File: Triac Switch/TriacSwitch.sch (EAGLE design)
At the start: 14 parts, among them T2 BT136

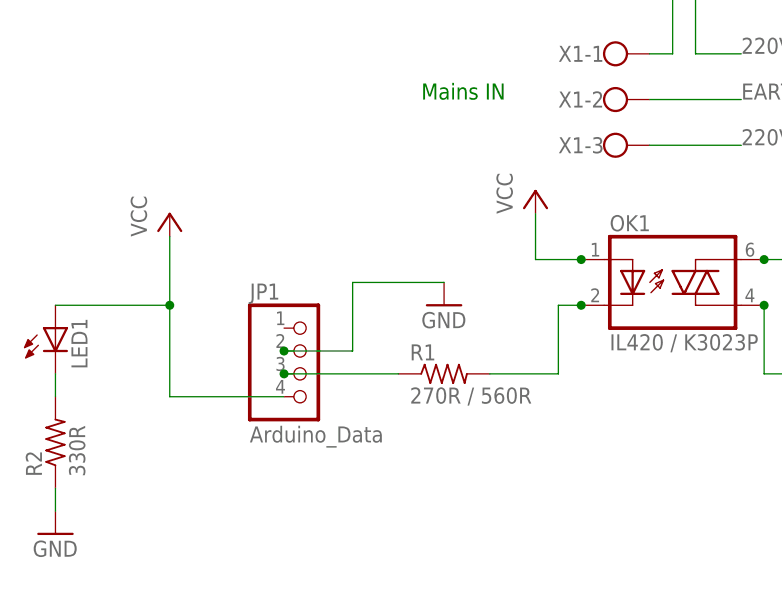
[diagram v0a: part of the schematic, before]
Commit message: Added Pinout to UD001 (Vishay) after successful test
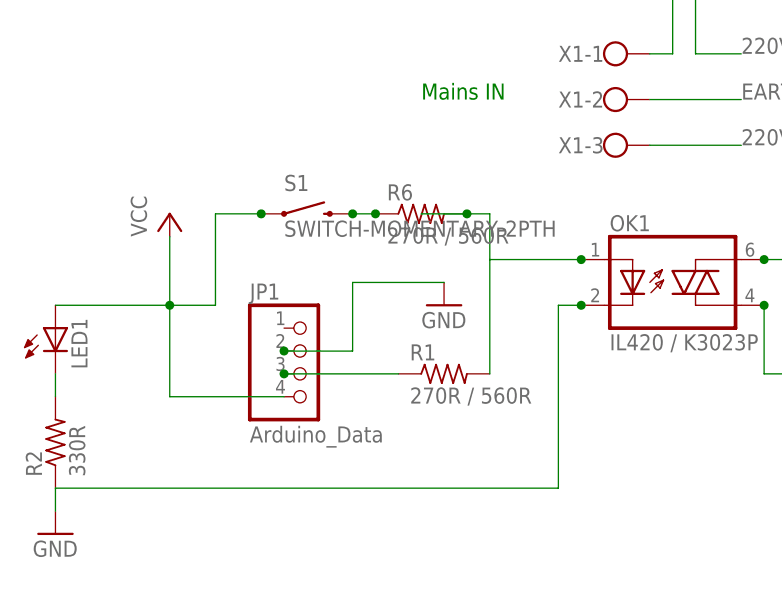
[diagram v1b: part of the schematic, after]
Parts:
- added R6: 270R / 560R, resistor:R-US_0207/10
- added S1: SWITCH-MOMENTARY-2PTH, SparkFun-Electromechanical:SWITCH-MOMENTARY-2PTH
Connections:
- removed net N$10: OK1.C, R1.2
- new net N$5: R6.1, S1.2
- new net N$8: OK1.A, R1.2, R6.2
- net GND: now also OK1.C
- net VCC: now also S1.1; no longer OK1.A
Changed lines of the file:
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@@
 <layers>
 <layer number="1" name="Top" color="4" fill="1" visible="no" active="no"/>
+<layer number="2" name="Route2" color="1" fill="3" visible="no" active="no"/>
+<layer number="3" name="Route3" color="4" fill="3" visible="no" active="no"/>
+<layer number="4" name="Route4" color="1" fill="4" visible="no" active="no"/>
+<layer number="5" name="Route5" color="4" fill="4" visible="no" active="no"/>
+<layer number="6" name="Route6" color="1" fill="8" visible="no" active="no"/>
+<layer number="7" name="Route7" color="4" fill="8" visible="no" active="no"/>
+<layer number="8" name="Route8" color="1" fill="2" visible="no" active="no"/>
+<layer number="9" name="Route9" color="4" fill="2" visible="no" active="no"/>
+<layer number="10" name="Route10" color="1" fill="7" visible="no" active="no"/>
+<layer number="11" name="Route11" color="4" fill="7" visible="no" active="no"/>
+<layer number="12" name="Route12" color="1" fill="5" visible="no" active="no"/>
+<layer number="13" name="Route13" color="4" fill="5" visible="no" active="no"/>
+<layer number="14" name="Route14" color="1" fill="6" visible="no" active="no"/>
+<layer number="15" name="Route15" color="4" fill="6" visible="no" active="no"/>
 <layer number="16" name="Bottom" color="1" fill="1" visible="no" active="no"/>
 <layer number="17" name="Pads" color="2" fill="1" visible="no" active="no"/>
@@
 <layer number="51" name="tDocu" color="7" fill="1" visible="no" active="no"/>
 <layer number="52" name="bDocu" color="7" fill="1" visible="no" active="no"/>
+<layer number="53" name="tGND_GNDA" color="7" fill="9" visible="no" active="no"/>
+<layer number="54" name="bGND_GNDA" color="1" fill="9" visible="no" active="no"/>
 <layer number="56" name="wert" color="7" fill="1" visible="no" active="no"/>
 <layer number="91" name="Nets" color="2" fill="1" visible="yes" active="yes"/>
@@
 <layer number="101" name="Gehäuse" color="7" fill="1" visible="no" active="yes"/>
 <layer number="102" name="Mittellin" color="7" fill="1" visible="no" active="yes"/>
+<layer number="103" name="tMap" color="7" fill="1" visible="no" active="yes"/>
 <layer number="104" name="Name" color="7" fill="1" visible="no" active="yes"/>
+<layer number="105" name="tPlate" color="7" fill="1" visible="no" active="yes"/>
+<layer number="106" name="bPlate" color="7" fill="1" visible="no" active="yes"/>
+<layer number="107" name="Crop" color="7" fill="1" visible="no" active="yes"/>
+<layer number="116" name="Patch_BOT" color="9" fill="4" visible="no" active="yes"/>
+<layer number="121" name="_tsilk" color="7" fill="1" visible="no" active="yes"/>
+<layer number="122" name="_bsilk" color="7" fill="1" visible="no" active="yes"/>
+<layer number="125" name="_tNames" color="7" fill="1" visible="no" active="yes"/>
+<layer number="144" name="Drill_legend" color="7" fill="1" visible="no" active="yes"/>
 <layer number="151" name="HeatSink" color="7" fill="1" visible="no" active="yes"/>
 <layer number="200" name="200bmp" color="1" fill="10" visible="no" active="no"/>
+<layer number="201" name="201bmp" color="2" fill="10" visible="no" active="yes"/>
+<layer number="202" name="202bmp" color="3" fill="10" visible="no" active="yes"/>
+<layer number="203" name="203bmp" color="4" fill="10" visible="no" active="yes"/>
+<layer number="204" name="204bmp" color="5" fill="10" visible="no" active="yes"/>
+<layer number="205" name="205bmp" color="6" fill="10" visible="no" active="yes"/>
+<layer number="206" name="206bmp" color="7" fill="10" visible="no" active="yes"/>
+<layer number="207" name="207bmp" color="8" fill="10" visible="no" active="yes"/>
+<layer number="208" name="208bmp" color="9" fill="10" visible="no" active="yes"/>
+<layer number="209" name="209bmp" color="7" fill="1" visible="no" active="yes"/>
+<layer number="210" name="210bmp" color="7" fill="1" visible="no" active="yes"/>
+<layer number="211" name="211bmp" color="7" fill="1" visible="no" active="yes"/>
+<layer number="212" name="212bmp" color="7" fill="1" visible="no" active="yes"/>
+<layer number="213" name="213bmp" color="7" fill="1" visible="no" active="yes"/>
+<layer number="214" name="214bmp" color="7" fill="1" visible="no" active="yes"/>
+<layer number="215" name="215bmp" color="7" fill="1" visible="no" active="yes"/>
+<layer number="216" name="216bmp" color="7" fill="1" visible="no" active="yes"/>
+<layer number="217" name="217bmp" color="18" fill="1" visible="no" active="no"/>
+<layer number="218" name="218bmp" color="19" fill="1" visible="no" active="no"/>
+<layer number="219" name="219bmp" color="20" fill="1" visible="no" active="no"/>
+<layer number="220" name="220bmp" color="21" fill="1" visible="no" active="no"/>
+<layer number="221" name="221bmp" color="22" fill="1" visible="no" active="no"/>
+<layer number="222" name="222bmp" color="23" fill="1" visible="no" active="no"/>
+<layer number="223" name="223bmp" color="24" fill="1" visible="no" active="no"/>
+<layer number="224" name="224bmp" color="25" fill="1" visible="no" active="no"/>
 <layer number="250" name="Descript" color="7" fill="1" visible="no" active="yes"/>
 <layer number="251" name="SMDround" color="7" fill="1" visible="no" active="yes"/>
@@
 <part name="JP1" library="pinhead" deviceset="PINHD-1X4" device="" value="Arduino_Data"/>
 <part name="P+1" library="supply1" deviceset="VCC" device=""/>
-<part name="P+2" library="supply1" deviceset="VCC" device=""/>
 <part name="GND1" library="supply1" deviceset="GND" device=""/>
 <part name="C1" library="cap-master" deviceset="CNP-" device="C050-110X055" value="100nF"/>
@@
 <part name="R5" library="resistor" deviceset="R-US_" device="0617/17" value="15K 5W"/>
 <part name="R3" library="resistor" deviceset="R-US_" device="0922/22" value="390R 10W"/>
+<part name="S1" library="SparkFun-Electromechanical" deviceset="SWITCH-MOMENTARY-2" device="PTH"/>
+<part name="R6" library="resistor" deviceset="R-US_" device="0207/10" value="270R / 560R"/>
 </parts>
 <sheets>
@@
 <instance part="JP1" gate="A" x="35.56" y="48.26"/>
 <instance part="P+1" gate="VCC" x="20.32" y="66.04"/>
-<instance part="P+2" gate="VCC" x="60.96" y="68.58"/>
 <instance part="GND1" gate="1" x="50.8" y="55.88"/>
 <instance part="C1" gate="G$1" x="139.7" y="50.8" rot="R90"/>
@@
 <instance part="R5" gate="G$1" x="99.06" y="60.96"/>
 <instance part="R3" gate="G$1" x="132.08" y="35.56" rot="R180"/>
+<instance part="S1" gate="G$1" x="35.56" y="66.04"/>
+<instance part="R6" gate="G$1" x="48.26" y="66.04"/>
 </instances>
 <busses>
@@
 <wire x1="7.62" y1="55.88" x2="20.32" y2="55.88" width="0.1524" layer="91"/>
 <junction x="20.32" y="55.88"/>
-</segment>
-<segment>
-<pinref part="OK1" gate="G$1" pin="A"/>
-<pinref part="P+2" gate="VCC" pin="VCC"/>
-<wire x1="66.04" y1="60.96" x2="60.96" y2="60.96" width="0.1524" layer="91"/>
-<wire x1="60.96" y1="60.96" x2="60.96" y2="66.04" width="0.1524" layer="91"/>
-<junction x="66.04" y="60.96"/>
+<wire x1="20.32" y1="55.88" x2="25.4" y2="55.88" width="0.1524" layer="91"/>
+<wire x1="25.4" y1="55.88" x2="25.4" y2="66.04" width="0.1524" layer="91"/>
+<pinref part="S1" gate="G$1" pin="1"/>
+<wire x1="25.4" y1="66.04" x2="30.48" y2="66.04" width="0.1524" layer="91"/>
+<junction x="30.48" y="66.04"/>
 </segment>
 </net>
@@
 <pinref part="R2" gate="G$1" pin="1"/>
 <pinref part="GND2" gate="1" pin="GND"/>
+<pinref part="OK1" gate="G$1" pin="C"/>
+<wire x1="66.04" y1="55.88" x2="63.5" y2="55.88" width="0.1524" layer="91"/>
+<junction x="66.04" y="55.88"/>
+<wire x1="63.5" y1="55.88" x2="63.5" y2="35.56" width="0.1524" layer="91"/>
+<wire x1="63.5" y1="35.56" x2="7.62" y2="35.56" width="0.1524" layer="91"/>
 <wire x1="7.62" y1="35.56" x2="7.62" y2="33.02" width="0.1524" layer="91"/>
 </segment>
@@
 </segment>
 </net>
-<net name="N$10" class="0">
-<segment>
-<pinref part="OK1" gate="G$1" pin="C"/>
-<wire x1="66.04" y1="55.88" x2="63.5" y2="55.88" width="0.1524" layer="91"/>
-<wire x1="63.5" y1="55.88" x2="63.5" y2="48.26" width="0.1524" layer="91"/>
-<junction x="66.04" y="55.88"/>
-<pinref part="R1" gate="G$1" pin="2"/>
-<wire x1="55.88" y1="48.26" x2="63.5" y2="48.26" width="0.1524" layer="91"/>
-</segment>
-</net>
 <net name="N$2" class="0">
 <segment>
@@
 </segment>
 </net>
+<net name="N$8" class="0">
+<segment>
+<pinref part="OK1" gate="G$1" pin="A"/>
+<junction x="66.04" y="60.96"/>
+<pinref part="R1" gate="G$1" pin="2"/>
+<wire x1="55.88" y1="48.26" x2="55.88" y2="60.96" width="0.1524" layer="91"/>
+<wire x1="66.04" y1="60.96" x2="55.88" y2="60.96" width="0.1524" layer="91"/>
+<wire x1="55.88" y1="60.96" x2="55.88" y2="66.04" width="0.1524" layer="91"/>
+<wire x1="55.88" y1="66.04" x2="53.34" y2="66.04" width="0.1524" layer="91"/>
+<pinref part="R6" gate="G$1" pin="2"/>
+<wire x1="53.34" y1="66.04" x2="48.26" y2="66.04" width="0.1524" layer="91"/>
+<junction x="53.34" y="66.04"/>
+</segment>
+</net>
+<net name="N$5" class="0">
+<segment>
+<pinref part="S1" gate="G$1" pin="2"/>
+<pinref part="R6" gate="G$1" pin="1"/>
+<wire x1="43.18" y1="66.04" x2="40.64" y2="66.04" width="0.1524" layer="91"/>
+<junction x="40.64" y="66.04"/>
+<junction x="43.18" y="66.04"/>
+</segment>
+</net>
